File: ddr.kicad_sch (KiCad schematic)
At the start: 27 parts, among them U801 MT41K256M16TW

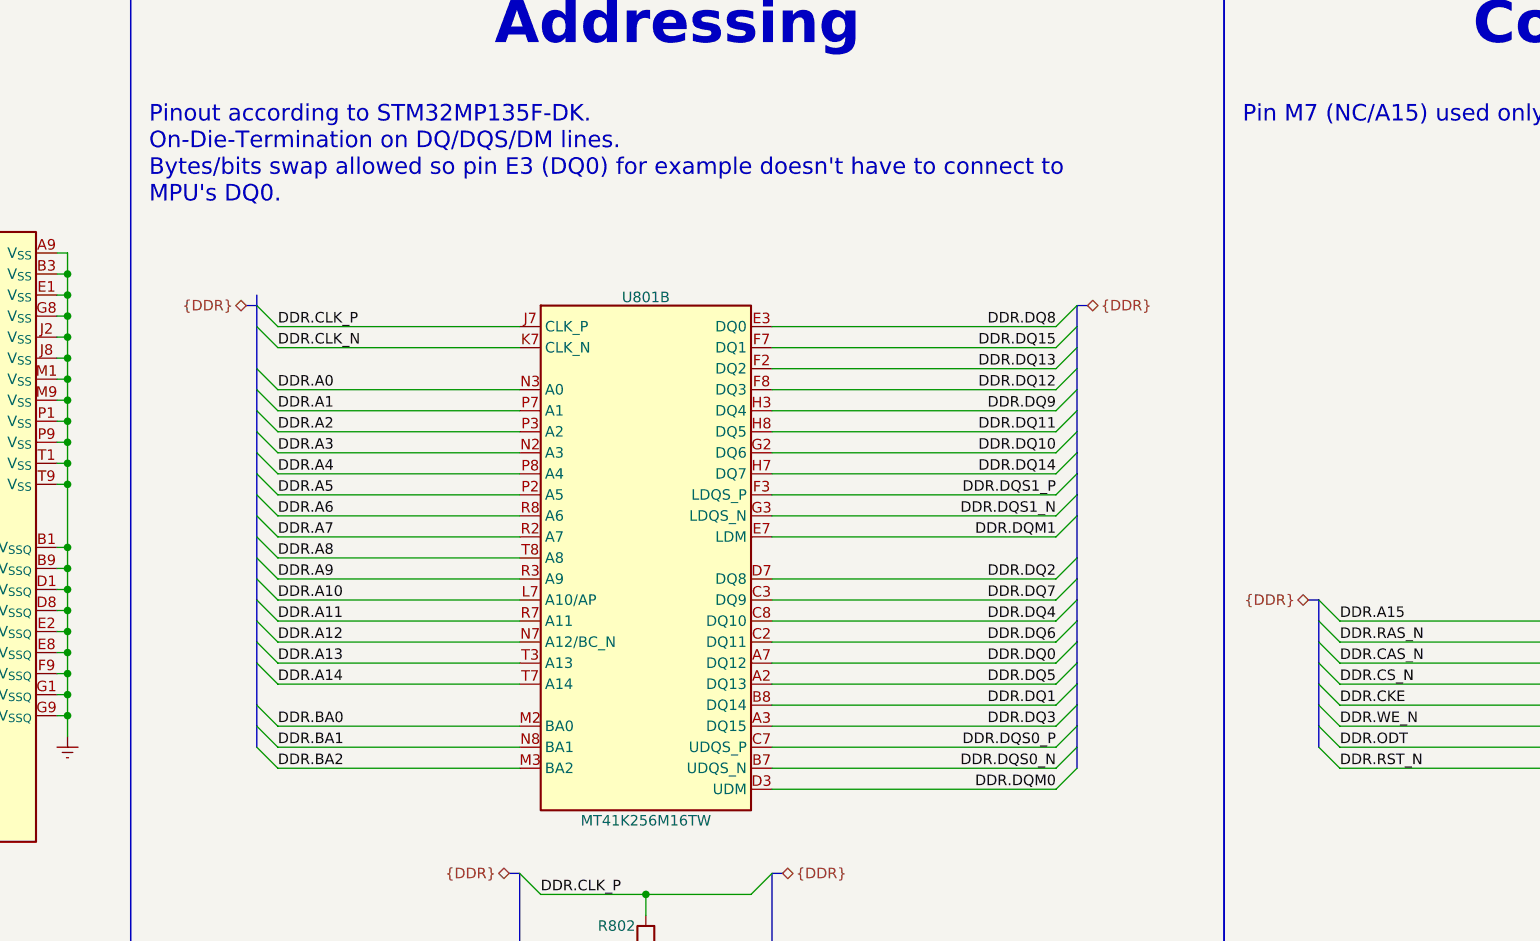
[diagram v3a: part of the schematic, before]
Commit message: Don't do bit swapping on DDR
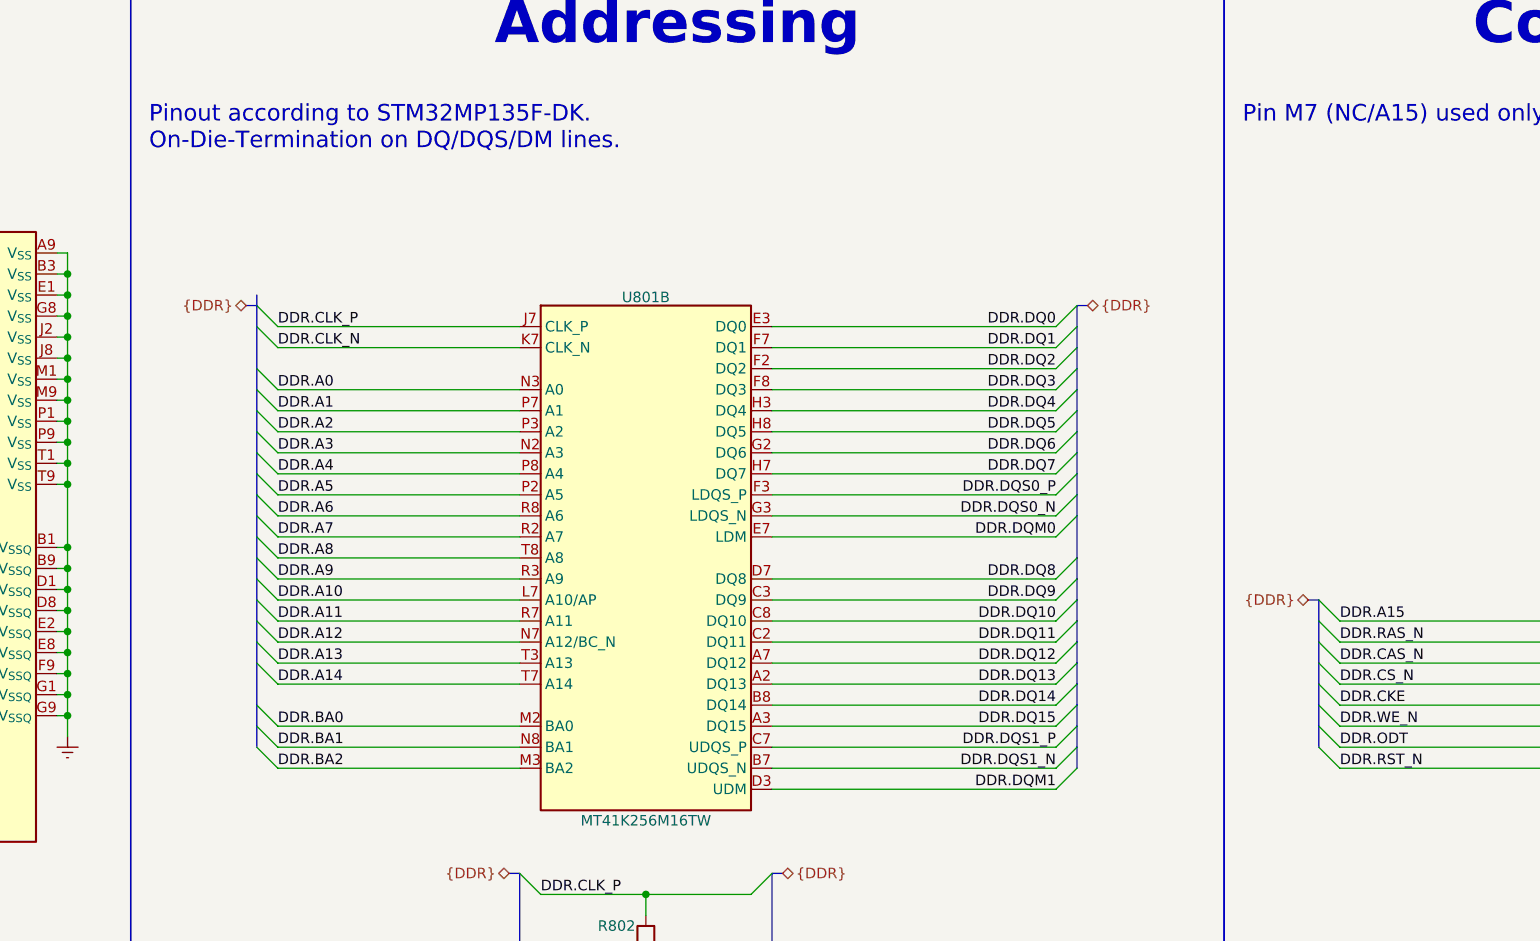
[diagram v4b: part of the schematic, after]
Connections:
- net DDR.DQ0: now also U801.E3 (DQ0); no longer U801.A7 (DQ12)
- net DDR.DQ1: now also U801.F7 (DQ1); no longer U801.B8 (DQ14)
- net DDR.DQ10: now also U801.C8 (DQ10); no longer U801.G2 (DQ6)
- net DDR.DQ11: now also U801.C2 (DQ11); no longer U801.H8 (DQ5)
- net DDR.DQ12: now also U801.A7 (DQ12); no longer U801.F8 (DQ3)
- net DDR.DQ13: now also U801.A2 (DQ13); no longer U801.F2 (DQ2)
- net DDR.DQ14: now also U801.B8 (DQ14); no longer U801.H7 (DQ7)
- net DDR.DQ15: now also U801.A3 (DQ15); no longer U801.F7 (DQ1)
- net DDR.DQ2: now also U801.F2 (DQ2); no longer U801.D7 (DQ8)
- net DDR.DQ3: now also U801.F8 (DQ3); no longer U801.A3 (DQ15)
- net DDR.DQ4: now also U801.H3 (DQ4); no longer U801.C8 (DQ10)
- net DDR.DQ5: now also U801.H8 (DQ5); no longer U801.A2 (DQ13)
- net DDR.DQ6: now also U801.G2 (DQ6); no longer U801.C2 (DQ11)
- net DDR.DQ7: now also U801.H7 (DQ7); no longer U801.C3 (DQ9)
- net DDR.DQ8: now also U801.D7 (DQ8); no longer U801.E3 (DQ0)
- net DDR.DQ9: now also U801.C3 (DQ9); no longer U801.H3 (DQ4)
- net DDR.DQM0: now also U801.E7 (LDM); no longer U801.D3 (UDM)
- net DDR.DQM1: now also U801.D3 (UDM); no longer U801.E7 (LDM)
- net DDR.DQS0_N: now also U801.G3 (LDQS_N); no longer U801.B7 (UDQS_N)
- net DDR.DQS0_P: now also U801.F3 (LDQS_P); no longer U801.C7 (UDQS_P)
- net DDR.DQS1_N: now also U801.B7 (UDQS_N); no longer U801.G3 (LDQS_N)
- net DDR.DQS1_P: now also U801.C7 (UDQS_P); no longer U801.F3 (LDQS_P)
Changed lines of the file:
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@@
 		)
 	)
-	(text_box "Pinout according to STM32MP135F-DK.\nOn-Die-Termination on DQ/DQS/DM lines.\nBytes/bits swap allowed so pin E3 (DQ0) for example doesn't have to connect to MPU's DQ0."
+	(text_box "Pinout according to STM32MP135F-DK.\nOn-Die-Termination on DQ/DQS/DM lines."
 		(exclude_from_sim no)
 		(at 186.69 63.5 0)
@@
 	)
 	(label "DDR.DQ13"
-		(at 297.18 96.52 180)
+		(at 297.18 134.62 180)
 		(effects
 			(font
@@
 	)
 	(label "DDR.DQM1"
-		(at 297.18 116.84 180)
+		(at 297.18 147.32 180)
 		(effects
 			(font
@@
 	)
 	(label "DDR.DQ6"
-		(at 297.18 129.54 180)
+		(at 297.18 106.68 180)
 		(effects
 			(font
@@
 	)
 	(label "DDR.DQS0_N"
-		(at 297.18 144.78 180)
+		(at 297.18 114.3 180)
 		(effects
 			(font
@@
 	)
 	(label "DDR.DQ7"
-		(at 297.18 124.46 180)
+		(at 297.18 109.22 180)
 		(effects
 			(font
@@
 	)
 	(label "DDR.DQ12"
-		(at 297.18 99.06 180)
+		(at 297.18 132.08 180)
 		(effects
 			(font
@@
 	)
 	(label "DDR.DQ14"
-		(at 297.18 109.22 180)
+		(at 297.18 137.16 180)
 		(effects
 			(font
@@
 	)
 	(label "DDR.DQ9"
-		(at 297.18 101.6 180)
+		(at 297.18 124.46 180)
 		(effects
 			(font
@@
 	)
 	(label "DDR.DQM0"
-		(at 297.18 147.32 180)
+		(at 297.18 116.84 180)
 		(effects
 			(font
@@
 	)
 	(label "DDR.DQ1"
-		(at 297.18 137.16 180)
+		(at 297.18 93.98 180)
 		(effects
 			(font
@@
 	)
 	(label "DDR.DQ5"
-		(at 297.18 134.62 180)
+		(at 297.18 104.14 180)
 		(effects
 			(font
@@
 	)
 	(label "DDR.DQS0_P"
-		(at 297.18 142.24 180)
+		(at 297.18 111.76 180)
 		(effects
 			(font
@@
 	)
 	(label "DDR.DQ11"
-		(at 297.18 104.14 180)
+		(at 297.18 129.54 180)
 		(effects
 			(font
@@
 	)
 	(label "DDR.DQ4"
-		(at 297.18 127 180)
+		(at 297.18 101.6 180)
 		(effects
 			(font
@@
 	)
 	(label "DDR.DQ0"
-		(at 297.18 132.08 180)
+		(at 297.18 91.44 180)
 		(effects
 			(font
@@
 	)
 	(label "DDR.DQ10"
-		(at 297.18 106.68 180)
+		(at 297.18 127 180)
 		(effects
 			(font
@@
 	)
 	(label "DDR.DQ2"
-		(at 297.18 121.92 180)
+		(at 297.18 96.52 180)
 		(effects
 			(font
@@
 	)
 	(label "DDR.DQ3"
-		(at 297.18 139.7 180)
+		(at 297.18 99.06 180)
 		(effects
 			(font
@@
 	)
 	(label "DDR.DQ15"
-		(at 297.18 93.98 180)
+		(at 297.18 139.7 180)
 		(effects
 			(font
@@
 	)
 	(label "DDR.DQS1_P"
-		(at 297.18 111.76 180)
+		(at 297.18 142.24 180)
 		(effects
 			(font
@@
 	)
 	(label "DDR.DQS1_N"
-		(at 297.18 114.3 180)
+		(at 297.18 144.78 180)
 		(effects
 			(font
@@
 	)
 	(label "DDR.DQ8"
-		(at 297.18 91.44 180)
+		(at 297.18 121.92 180)
 		(effects
 			(font

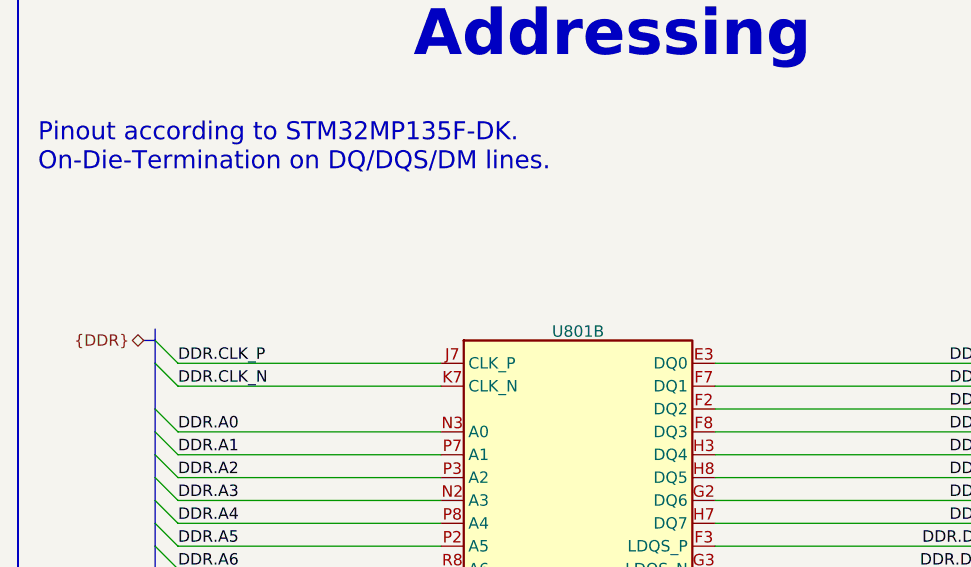
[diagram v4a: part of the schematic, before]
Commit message: Redo MPU pinout using STM32CubeMx
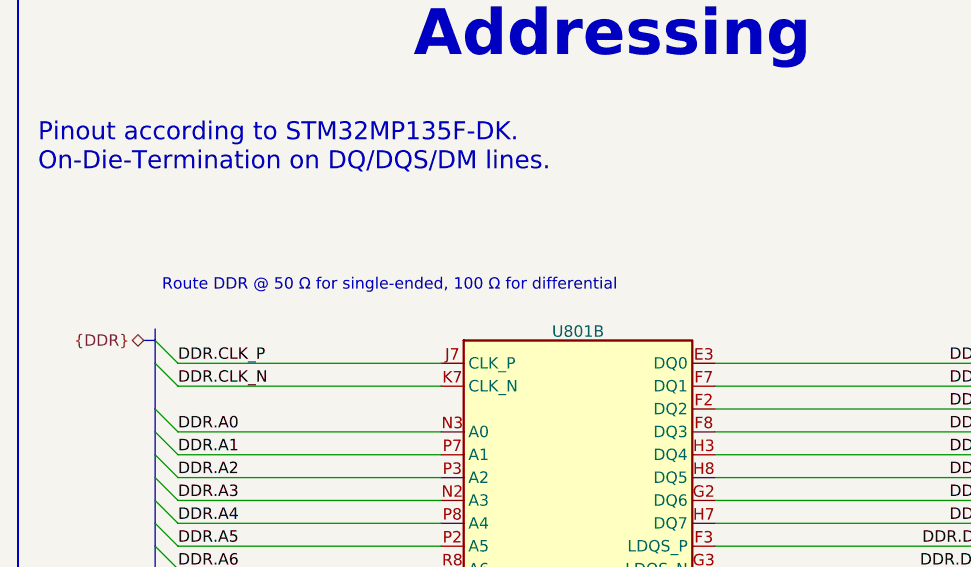
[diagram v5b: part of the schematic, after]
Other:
- note added: "Route DDR @ 50 Ω for single-ended, 100 Ω for differential"
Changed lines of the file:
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@@
 		(rev "v0.0.1")
+	)
+	(text "Route DDR @ 50 Ω for single-ended, 100 Ω for differential"
+		(exclude_from_sim no)
+		(at 201.422 82.804 0)
+		(effects
+			(font
+				(size 1.27 1.27)
+				(color 194 0 194 1)
+			)
+			(justify left)
+		)
 	)
 	(text_box "Notes"

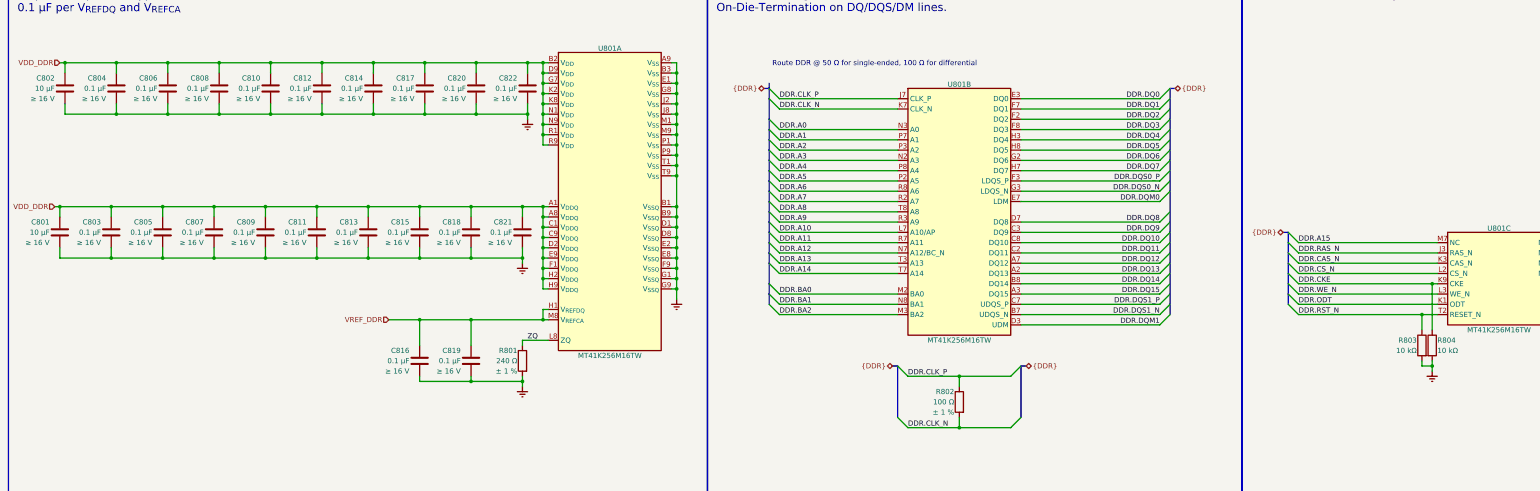
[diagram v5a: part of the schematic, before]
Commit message: Add additional info to passives
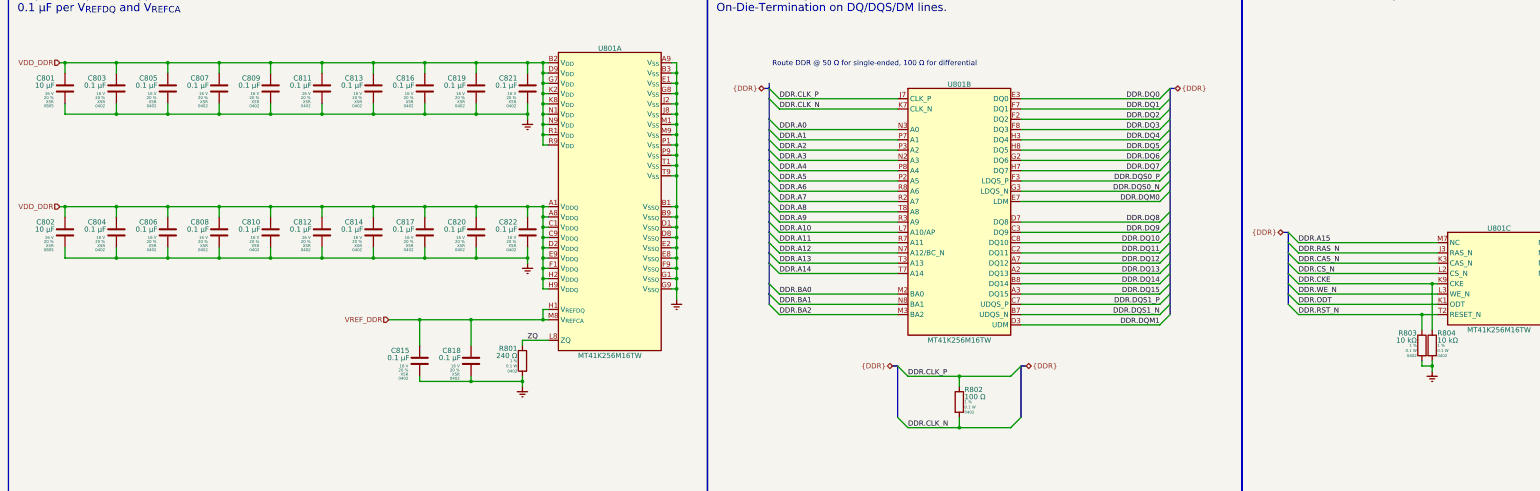
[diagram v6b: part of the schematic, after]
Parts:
- C801, C802: Size (none) -> 0805; Temperature coefficient (none) -> X5R; Tolerance (none) -> 20 %; Voltage rating ≥ 16 V -> 16 V
- C803, C804, C805, C806, C807, C808, C809, C810, C811, C812, C813, C814, C815, C816, C817, C818, C819, C820, C821, C822: Size (none) -> 0402; Temperature coefficient (none) -> X5R; Tolerance (none) -> 20 %; Voltage rating ≥ 16 V -> 16 V
- R801, R802: Power rating (none) -> 0.1 W; Size (none) -> 0402; Tolerance ± 1 % -> 1 %
- R803, R804: MPN 560112110020 -> (none); Manufacturer Würth Elektronik -> (none); Power rating (none) -> 0.1 W; Size (none) -> 0402; Tolerance (none) -> 1 %
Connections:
- net VDD_DDR: now also C816.1, C819.1; no longer C815.1, C818.1
- net VREF_DDR: now also C815.1, C818.1; no longer C816.1, C819.1

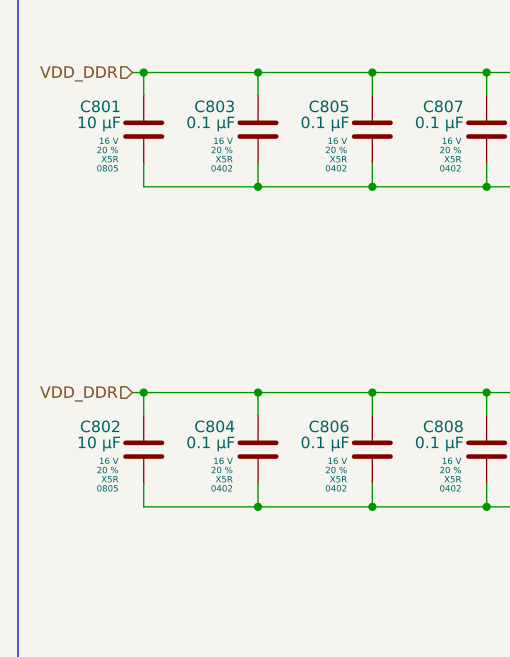
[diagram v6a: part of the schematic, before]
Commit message: Update capacitor BOM
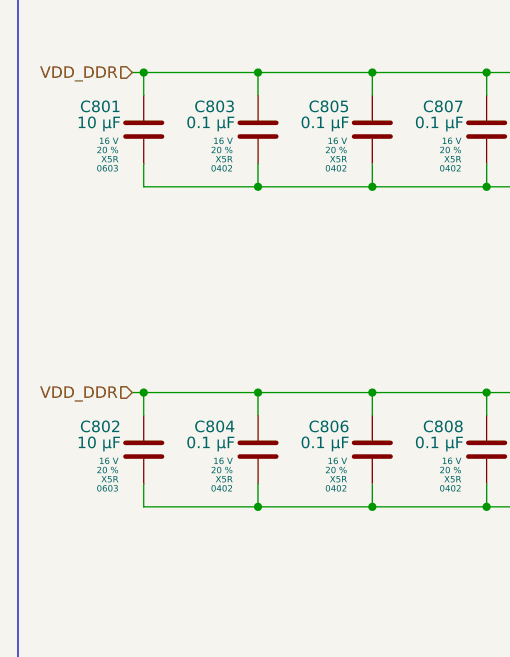
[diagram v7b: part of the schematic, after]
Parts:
- C801, C802: footprint (none) -> Capacitor_SMD:C_0603_1608Metric; Digi-Key Part Number (none) -> 490-13248-1-ND; MPN (none) -> GRM188R6YA106MA73D; Manufacturer (none) -> Murata Electronics; Size 0805 -> 0603
- C803, C804, C805, C806, C807, C808, C809, C810, C811, C812, C813, C814, C815, C816, C817, C818, C819, C820, C821, C822: footprint (none) -> perfect_footprints:C_0402_1005Metric; Digi-Key Part Number (none) -> 490-10700-1-ND; MPN (none) -> GRM155R71H104KE14D; Manufacturer (none) -> Murata Electronics

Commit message: Update R & L BOM
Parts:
- R801: Digi-Key Part Number (none) -> P240LCT-ND; MPN (none) -> ERJ-2RKF2400X; Manufacturer (none) -> Panasonic Electronic Components
- R802: Digi-Key Part Number (none) -> P100LCT-ND; MPN (none) -> ERJ-2RKF1000X; Manufacturer (none) -> Panasonic Electronic Components
- R803, R804: Digi-Key Part Number (none) -> P10.0KLCT-ND; MPN (none) -> ERJ-2RKF1002X; Manufacturer (none) -> Panasonic Electronic Components
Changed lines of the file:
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@@
 			)
 		)
-		(property "Datasheet" "https://www.we-online.com/components/products/datasheet/560112116014.pdf"
+		(property "Datasheet" "https://industrial.panasonic.com/cdbs/www-data/pdf/RDA0000/AOA0000C304.pdf"
 			(at 361.95 152.4 0)
 			(effects
@@
 			)
 		)
-		(property "Description" "Resistor"
+		(property "Description" "10 kOhms ±1% 0.1W, 1/10W Chip Resistor 0402 (1005 Metric) Automotive AEC-Q200 Thick Film"
 			(at 361.95 152.4 0)
 			(effects
@@
 			)
 		)
-		(property "MPN" ""
+		(property "MPN" "ERJ-2RKF1002X"
 			(at 361.95 152.4 0)
 			(effects
@@
 			)
 		)
-		(property "Manufacturer" ""
+		(property "Manufacturer" "Panasonic Electronic Components"
 			(at 361.95 152.4 0)
 			(effects
@@
 			)
 		)
+		(property "Digi-Key Part Number" "P10.0KLCT-ND"
+			(at 361.95 152.4 0)
+			(effects
+				(font
+					(size 1.27 1.27)
+				)
+				(hide yes)
+			)
+		)
 		(pin "2"
 		)
@@
 			)
 		)
-		(property "Datasheet" "https://www.we-online.com/components/products/datasheet/560112116014.pdf"
+		(property "Datasheet" "https://industrial.panasonic.com/cdbs/www-data/pdf/RDA0000/AOA0000C304.pdf"
 			(at 247.65 166.37 0)
 			(effects
@@
 			)
 		)
-		(property "Description" "Resistor"
+		(property "Description" "100 Ohms ±1% 0.1W, 1/10W Chip Resistor 0402 (1005 Metric) Automotive AEC-Q200 Thick Film"
 			(at 247.65 166.37 0)
 			(effects
@@
 			)
 		)
-		(property "MPN" ""
+		(property "MPN" "ERJ-2RKF1000X"
 			(at 247.65 166.37 0)
 			(effects
@@
 			)
 		)
-		(property "Manufacturer" ""
+		(property "Manufacturer" "Panasonic Electronic Components"
 			(at 247.65 166.37 0)
 			(effects
@@
 			)
 		)
+		(property "Digi-Key Part Number" "P100LCT-ND"
+			(at 247.65 166.37 0)
+			(effects
+				(font
+					(size 1.27 1.27)
+				)
+				(hide yes)
+			)
+		)
 		(pin "2"
 		)
@@
 			)
 		)
-		(property "Datasheet" "https://www.we-online.com/components/products/datasheet/560112116014.pdf"
+		(property "Datasheet" "https://industrial.panasonic.com/cdbs/www-data/pdf/RDA0000/AOA0000C304.pdf"
 			(at 364.49 152.4 0)
 			(effects
@@
 			)
 		)
-		(property "Description" "Resistor"
+		(property "Description" "10 kOhms ±1% 0.1W, 1/10W Chip Resistor 0402 (1005 Metric) Automotive AEC-Q200 Thick Film"
 			(at 364.49 152.4 0)
 			(effects
@@
 			)
 		)
-		(property "MPN" ""
+		(property "MPN" "ERJ-2RKF1002X"
 			(at 364.49 152.4 0)
 			(effects
@@
 			)
 		)
-		(property "Manufacturer" ""
+		(property "Manufacturer" "Panasonic Electronic Components"
 			(at 364.49 152.4 0)
 			(effects
@@
 			)
 		)
+		(property "Digi-Key Part Number" "P10.0KLCT-ND"
+			(at 364.49 152.4 0)
+			(effects
+				(font
+					(size 1.27 1.27)
+				)
+				(hide yes)
+			)
+		)
 		(pin "2"
 		)
@@
 			)
 		)
-		(property "Datasheet" "https://www.we-online.com/components/products/datasheet/560112116014.pdf"
+		(property "Datasheet" "https://industrial.panasonic.com/cdbs/www-data/pdf/RDA0000/AOA0000C304.pdf"
 			(at 139.7 156.21 0)
 			(effects
@@
 			)
 		)
-		(property "Description" "Resistor"
+		(property "Description" "240 Ohms ±1% 0.1W, 1/10W Chip Resistor 0402 (1005 Metric) Automotive AEC-Q200 Thick Film"
 			(at 139.7 156.21 0)
 			(effects
@@
 			)
 		)
-		(property "MPN" ""
+		(property "MPN" "ERJ-2RKF2400X"
 			(at 139.7 156.21 0)
 			(effects
@@
 			)
 		)
-		(property "Manufacturer" ""
+		(property "Manufacturer" "Panasonic Electronic Components"
 			(at 139.7 156.21 0)
 			(effects
@@
 			)
 		)
+		(property "Digi-Key Part Number" "P240LCT-ND"
+			(at 139.7 156.21 0)
+			(effects
+				(font
+					(size 1.27 1.27)
+				)
+				(hide yes)
+			)
+		)
